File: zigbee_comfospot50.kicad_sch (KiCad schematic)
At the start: 2 parts, among them U1 ESP32-H2-WROOM-02C

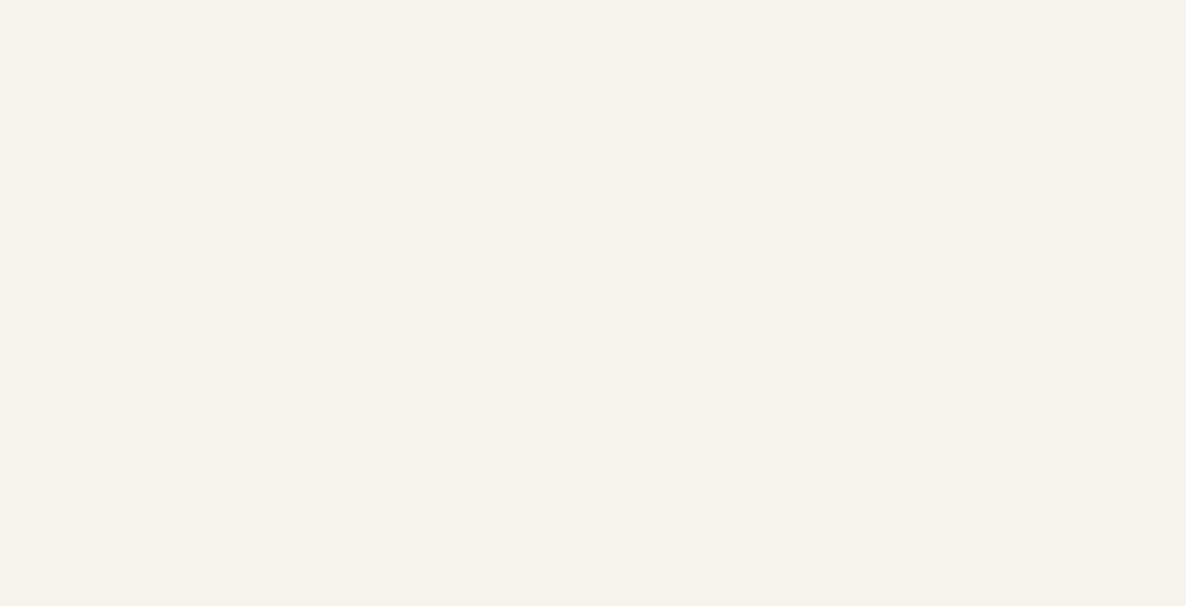
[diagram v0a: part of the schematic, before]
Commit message: added signal names
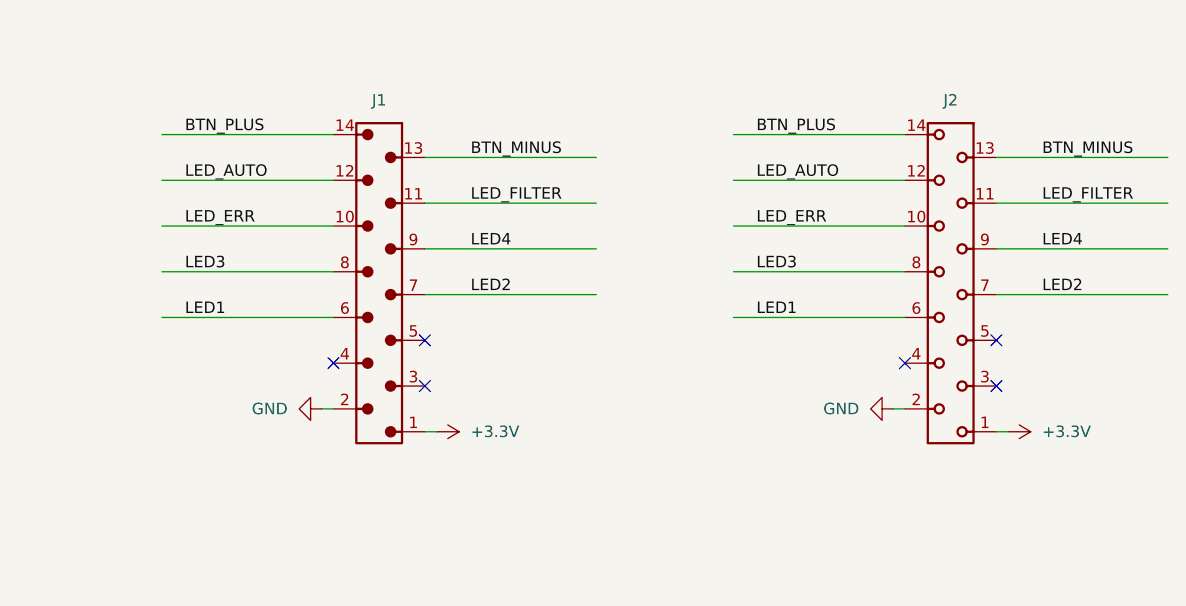
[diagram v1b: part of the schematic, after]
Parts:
- added J1: 690357101472, Connector_THT_Wurth:J_Wurth_WR-MM_690357101472, symbol local:690357101472
- added J2: 690368191472, Connector_THT_Wurth:J_Wurth_WR-MM_690368191472, symbol local:690368191472
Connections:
- new net +3.3V: J1.1, J2.1
- new net BTN_MINUS: J1.13, J2.13
- new net BTN_PLUS: J1.14, J2.14
- new net GND: J1.2, J2.2
- new net LED1: J1.6, J2.6
- new net LED2: J1.7, J2.7
- new net LED3: J1.8, J2.8
- new net LED4: J1.9, J2.9
- new net LED_AUTO: J1.12, J2.12
- new net LED_ERR: J1.10, J2.10
- new net LED_FILTER: J1.11, J2.11
- no-connect marks 0 -> 6

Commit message: 3D model
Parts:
- added C1, C2: 10uF, Capacitor_SMD:C_1206_3216Metric, symbol Device:C
- added J3: Conn_01x04, Connector_PinHeader_2.54mm:PinHeader_1x04_P2.54mm_Vertical, symbol Connector_Generic:Conn_01x04
- added R1: 1R, Capacitor_SMD:C_0805_2012Metric, symbol Device:R
- added R2: 1k, Capacitor_SMD:C_0805_2012Metric, symbol Device:R
- added SW1: SW_Push, Button_Switch_THT:SW_PUSH_6mm, symbol Switch:SW_Push
- U1: footprint (none) -> local:ESP32-H2-WROOM-02C
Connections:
- net +3.3V: now also J3.1 (Pin_1), R1.1, R2.1
- net GND: now also M1.13 (GND), M1.29 (GND), M1.30 (GND), M1.9 (GND), C1.2, C2.2, J3.4 (Pin_4), SW1.1
- net at M1.2 (EN): now also R2.2, SW1.2
- net RXD: now reaches M1.21 (RXD0)
- net RXD: now also J3.2 (Pin_2)
- net TXD: now reaches M1.22 (TXD0)
- net TXD: now also J3.3 (Pin_3)
- net at M1.1 (3V3): now also C1.1, C2.1, R1.2
- no-connect marks 6 -> 7

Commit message: Started routing
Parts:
- removed J2: 690368191472, Connector_THT_Wurth:J_Wurth_WR-MM_690368191472, symbol local:690368191472
- added J2: 690367191472, J_Wurth_WR-MM_690367191472, symbol local:690367191472
- added R10, R11, R5, R6, R7, R8, R9: 47k, Resistor_SMD:R_0805_2012Metric, symbol Device:R
- added R3, R4: 10k, Resistor_SMD:R_0805_2012Metric, symbol Device:R
- added SW2: SW_Push, Button_Switch_SMD:SW_Push_1P1T_NO_CK_KSC7xxJ, symbol Switch:SW_Push
- R1: footprint Capacitor_SMD:C_0805_2012Metric -> Resistor_SMD:R_0805_2012Metric
- R2: value 1k -> 10k; footprint Capacitor_SMD:C_0805_2012Metric -> Resistor_SMD:R_0805_2012Metric
- SW1: footprint Button_Switch_THT:SW_PUSH_6mm -> Button_Switch_SMD:SW_Push_1P1T_NO_CK_KSC7xxJ
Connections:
- net +3.3V: now also J2.1, R10.1, R11.1, R3.1, R4.1, R5.1, R6.1, R7.1, R8.1, R9.1
- net BTN_MINUS: now also U1.27 (IO1), J2.13
- net BTN_PLUS: now also U1.28 (IO0), J2.14
- net GND: now also J2.2, SW2.1
- net LED1: now also U1.11 (IO13), J2.6, R8.2
- net LED2: now also U1.12 (IO14), J2.7, R9.2
- net LED3: now also U1.15 (IO22), J2.8, R10.2
- net LED4: now also U1.20 (IO25), J2.9, R11.2
- net LED_AUTO: now also U1.5 (IO10), J2.12, R5.2
- net LED_ERR: now also U1.10 (IO12), J2.10, R7.2
- net LED_FILTER: now also U1.6 (IO11), J2.11, R6.2
- net RXD: now also J3.3 (Pin_3); no longer J3.2 (Pin_2)
- net TXD: now also J3.2 (Pin_2); no longer J3.3 (Pin_3)
- net GPIO8_BOOT: now reaches U1.7 (IO8)
- net GPIO8_BOOT: now also R3.2
- net GPIO9_BOOT: now reaches U1.8 (IO9)
- net GPIO9_BOOT: now also R4.2, SW2.2

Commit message: ROuted
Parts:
- J1: footprint Connector_THT_Wurth:J_Wurth_WR-MM_690357101472 -> J_Wurth_WR-MM_690357101472
- U1: renamed from M1; value ~ -> ESP32-H2-WROOM-02C
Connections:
- net BTN_MINUS: now also U1.28 (IO0); no longer U1.27 (IO1)
- net BTN_PLUS: now also U1.27 (IO1); no longer U1.28 (IO0)
- net LED1: now also U1.20 (IO25); no longer U1.11 (IO13)
- net LED2: now also U1.15 (IO22); no longer U1.12 (IO14)
- net LED3: now also U1.12 (IO14); no longer U1.15 (IO22)
- net LED4: now also U1.11 (IO13); no longer U1.20 (IO25)
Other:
- moved on the sheet: R10, R11, R8, R9
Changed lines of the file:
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@@
 		)
 	)
-	(label "BTN_MINUS"
-		(at 111.76 111.76 0)
+	(label "LED4"
+		(at 111.76 137.16 0)
 		(effects
 			(font
@@
 	)
 	(label "LED3"
-		(at 111.76 142.24 0)
+		(at 111.76 139.7 0)
 		(effects
 			(font
@@
 		)
 	)
-	(label "LED2"
-		(at 111.76 139.7 0)
+	(label "BTN_PLUS"
+		(at 111.76 111.76 0)
 		(effects
 			(font
@@
 		)
 	)
+	(label "BTN_MINUS"
+		(at 111.76 109.22 0)
+		(effects
+			(font
+				(size 1.27 1.27)
+			)
+			(justify left bottom)
+		)
+	)
 	(label "LED_FILTER"
 		(at 250.19 57.15 0)
@@
 		)
 	)
-	(label "LED1"
-		(at 111.76 137.16 0)
-		(effects
-			(font
-				(size 1.27 1.27)
-			)
-			(justify left bottom)
-		)
-	)
-	(label "BTN_PLUS"
-		(at 111.76 109.22 0)
-		(effects
-			(font
-				(size 1.27 1.27)
-			)
-			(justify left bottom)
-		)
-	)
 	(label "BTN_PLUS"
 		(at 218.44 49.53 0)
@@
 	)
 	(label "LED1"
+		(at 111.76 144.78 0)
+		(effects
+			(font
+				(size 1.27 1.27)
+			)
+			(justify left bottom)
+		)
+	)
+	(label "LED1"
 		(at 218.44 69.85 0)
 		(effects
@@
 		)
 	)
+	(label "LED2"
+		(at 111.76 142.24 0)
+		(effects
+			(font
+				(size 1.27 1.27)
+			)
+			(justify left bottom)
+		)
+	)
 	(label "LED_FILTER"
 		(at 186.69 57.15 0)
@@
 	(label "LED_AUTO"
 		(at 218.44 54.61 0)
-		(effects
-			(font
-				(size 1.27 1.27)
-			)
-			(justify left bottom)
-		)
-	)
-	(label "LED4"
-		(at 111.76 144.78 0)
 		(effects
 			(font
@@
 		(on_board yes)
 		(dnp no)
-		(fields_autoplaced yes)
-		(property "Reference" "M1"
+		(property "Reference" "U1"
 			(at 80.01 34.29 0)
 			(effects
@@
 			)
 		)
-		(property "Value" "~"
-			(at 91.44 35.56 0)
+		(property "Value" "ESP32-H2-WROOM-02C"
+			(at 74.93 27.94 0)
 			(effects
 				(font
@@
 			(project ""
 				(path "/d343b823-46f1-4a7e-8d07-ec772fdffc11"
-					(reference "M1")
+					(reference "U1")
 					(unit 4)
 				)
@@
 			)
 		)
-		(property "Footprint" "Connector_THT_Wurth:J_Wurth_WR-MM_690357101472"
+		(property "Footprint" "J_Wurth_WR-MM_690357101472"
 			(at 191.77 66.04 0)
 			(effects
@@
 		(on_board yes)
 		(dnp no)
-		(fields_autoplaced yes)
-		(property "Reference" "M1"
+		(property "Reference" "U1"
 			(at 63.5 76.2 0)
 			(effects
@@
 			)
 		)
-		(property "Value" "~"
-			(at 74.93 74.93 0)
+		(property "Value" "ESP32-H2-WROOM-02C"
+			(at 58.166 67.056 0)
 			(effects
 				(font
@@
 			(project ""
 				(path "/d343b823-46f1-4a7e-8d07-ec772fdffc11"
-					(reference "M1")
+					(reference "U1")
 					(unit 3)
 				)
@@
 	(symbol
 		(lib_id "Device:R")
-		(at 101.6 142.24 90)
+		(at 101.6 139.7 90)
 		(unit 1)
 		(exclude_from_sim no)
@@
 		(dnp no)
 		(property "Reference" "R10"
-			(at 96.266 141.224 90)
+			(at 96.266 138.684 90)
 			(effects
 				(font
@@
 		)
 		(property "Value" "47k"
-			(at 107.442 140.97 90)
+			(at 107.442 138.43 90)
 			(effects
 				(font
@@
 		)
 		(property "Footprint" "Resistor_SMD:R_0805_2012Metric"
-			(at 101.6 144.018 90)
+			(at 101.6 141.478 90)
 			(effects
 				(font
@@
 		)
 		(property "Datasheet" "~"
-			(at 101.6 142.24 0)
+			(at 101.6 139.7 0)
 			(effects
 				(font
@@
 		)
 		(property "Description" "Resistor"
-			(at 101.6 142.24 0)
+			(at 101.6 139.7 0)
 			(effects
 				(font
@@
 	(symbol
 		(lib_id "Device:R")
-		(at 101.6 144.78 90)
+		(at 101.6 137.16 90)
 		(unit 1)
 		(exclude_from_sim no)
@@
 		(dnp no)
 		(property "Reference" "R11"
-			(at 96.266 143.764 90)
+			(at 96.266 136.144 90)
 			(effects
 				(font
@@
 		)
 		(property "Value" "47k"
-			(at 107.442 143.51 90)
+			(at 107.442 135.89 90)
 			(effects
 				(font
@@
 		)
 		(property "Footprint" "Resistor_SMD:R_0805_2012Metric"
-			(at 101.6 146.558 90)
+			(at 101.6 138.938 90)
 			(effects
 				(font
@@
 		)
 		(property "Datasheet" "~"
-			(at 101.6 144.78 0)
+			(at 101.6 137.16 0)
 			(effects
 				(font
@@
 		)
 		(property "Description" "Resistor"
-			(at 101.6 144.78 0)
+			(at 101.6 137.16 0)
 			(effects
 				(font
@@
 		(on_board yes)
 		(dnp no)
-		(fields_autoplaced yes)
-		(property "Reference" "M1"
+		(property "Reference" "U1"
 			(at 62.23 35.56 0)
 			(effects
@@
 			)
 		)
-		(property "Value" "~"
-			(at 73.66 35.56 0)
+		(property "Value" "ESP32-H2-WROOM-02C"
+			(at 57.658 21.59 0)
 			(effects
 				(font
@@
 				)
 				(justify left)
+				(hide yes)
 			)
 		)
@@
 			(project ""
 				(path "/d343b823-46f1-4a7e-8d07-ec772fdffc11"
-					(reference "M1")
+					(reference "U1")
 					(unit 2)
 				)
@@
 	(symbol
 		(lib_id "Device:R")
-		(at 101.6 139.7 90)
+		(at 101.6 142.24 90)
 		(unit 1)
 		(exclude_from_sim no)
@@
 		(dnp no)
 		(property "Reference" "R9"
-			(at 95.758 138.684 90)
+			(at 95.758 141.224 90)
 			(effects
 				(font
@@
 		)
 		(property "Value" "47k"
-			(at 107.442 138.43 90)
+			(at 107.442 140.97 90)
 			(effects
 				(font
@@
 		)
 		(property "Footprint" "Resistor_SMD:R_0805_2012Metric"
-			(at 101.6 141.478 90)
+			(at 101.6 144.018 90)
 			(effects
 				(font
@@
 		)
 		(property "Datasheet" "~"
-			(at 101.6 139.7 0)
+			(at 101.6 142.24 0)
 			(effects
 				(font
@@
 		)
 		(property "Description" "Resistor"
-			(at 101.6 139.7 0)
+			(at 101.6 142.24 0)
 			(effects
 				(font
@@
 	(symbol
 		(lib_id "Device:R")
-		(at 101.6 137.16 90)
+		(at 101.6 144.78 90)
 		(unit 1)
 		(exclude_from_sim no)
@@
 		(dnp no)
 		(property "Reference" "R8"
-			(at 95.758 136.144 90)
+			(at 95.758 143.764 90)
 			(effects
 				(font
@@
 		)
 		(property "Value" "47k"
-			(at 107.442 135.89 90)
+			(at 107.442 143.51 90)
 			(effects
 				(font
@@
 		)
 		(property "Footprint" "Resistor_SMD:R_0805_2012Metric"
-			(at 101.6 138.938 90)
+			(at 101.6 146.558 90)
 			(effects
 				(font
@@
 		)
 		(property "Datasheet" "~"
-			(at 101.6 137.16 0)
+			(at 101.6 144.78 0)
 			(effects
 				(font
@@
 		)
 		(property "Description" "Resistor"
-			(at 101.6 137.16 0)
-			(effects
-				(font
+			(at 101.6 144.78 0)
+			(effects
+				(font
